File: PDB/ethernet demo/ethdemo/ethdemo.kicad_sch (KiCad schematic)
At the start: 100 parts, among them J1 0826-1X1T-GJ-F, J2 0826-1X1T-GJ-F, J3 Conn_01x05_Socket, J4 2171790001, Q1 CSD19538Q3AT, U1 STM32H742VGTx, U2 KSZ8863RLLI, U3 TPS23861PWR, Y1 25MHz

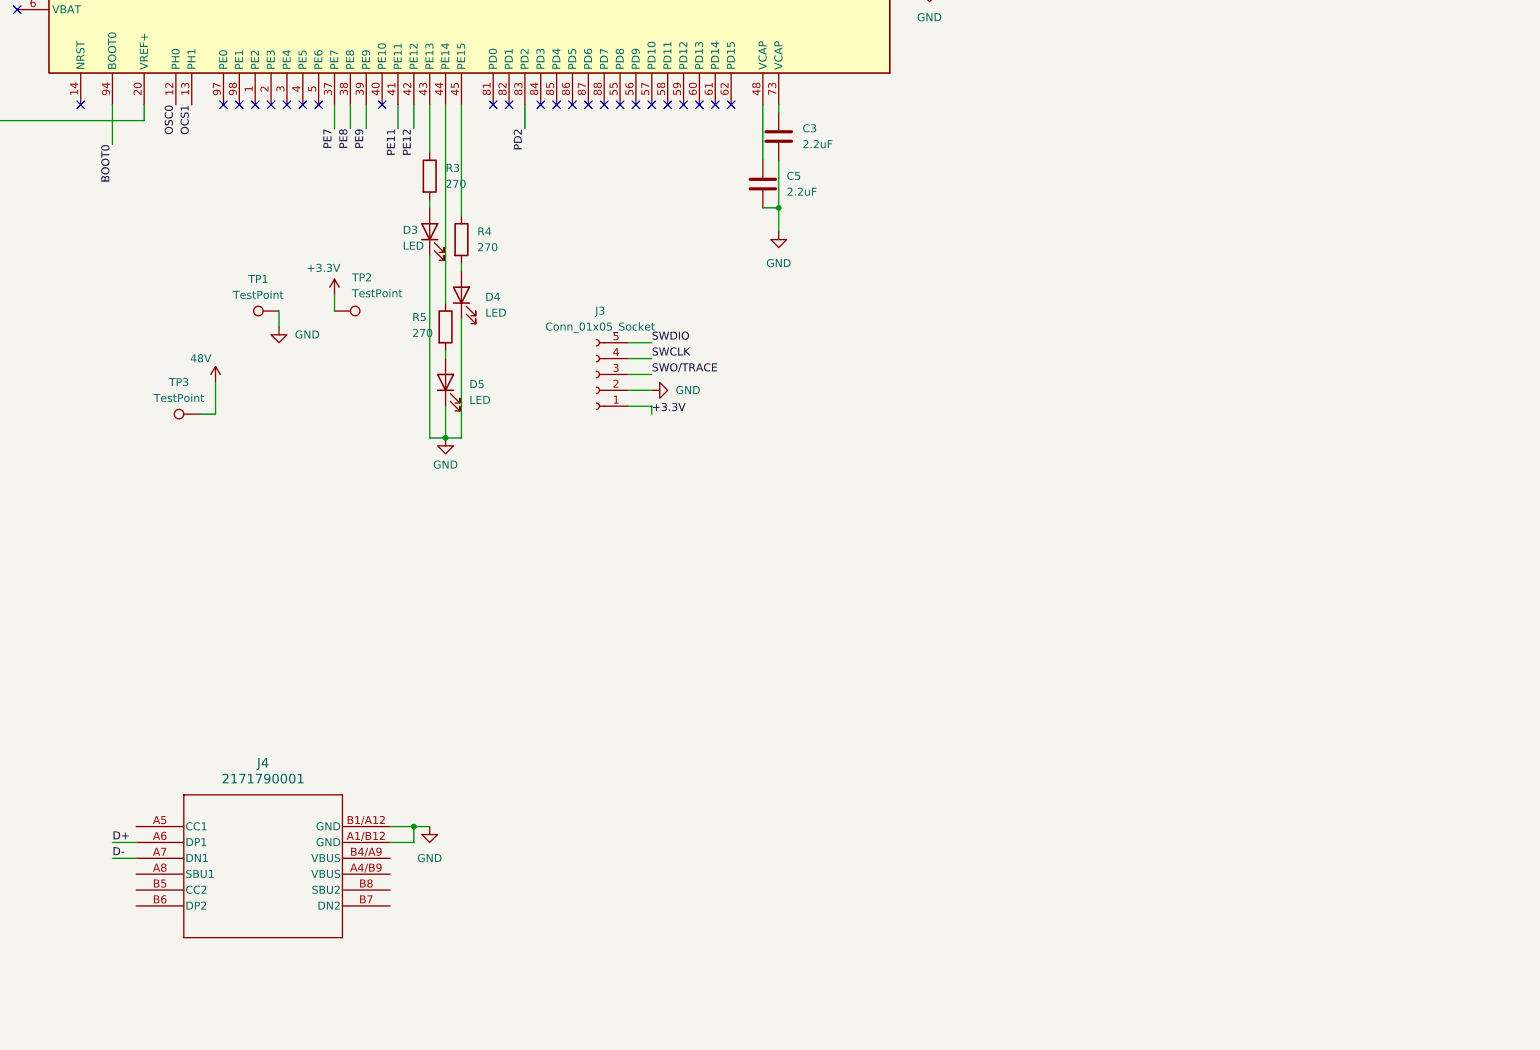
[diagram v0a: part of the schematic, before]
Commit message: routed usb and added power pads
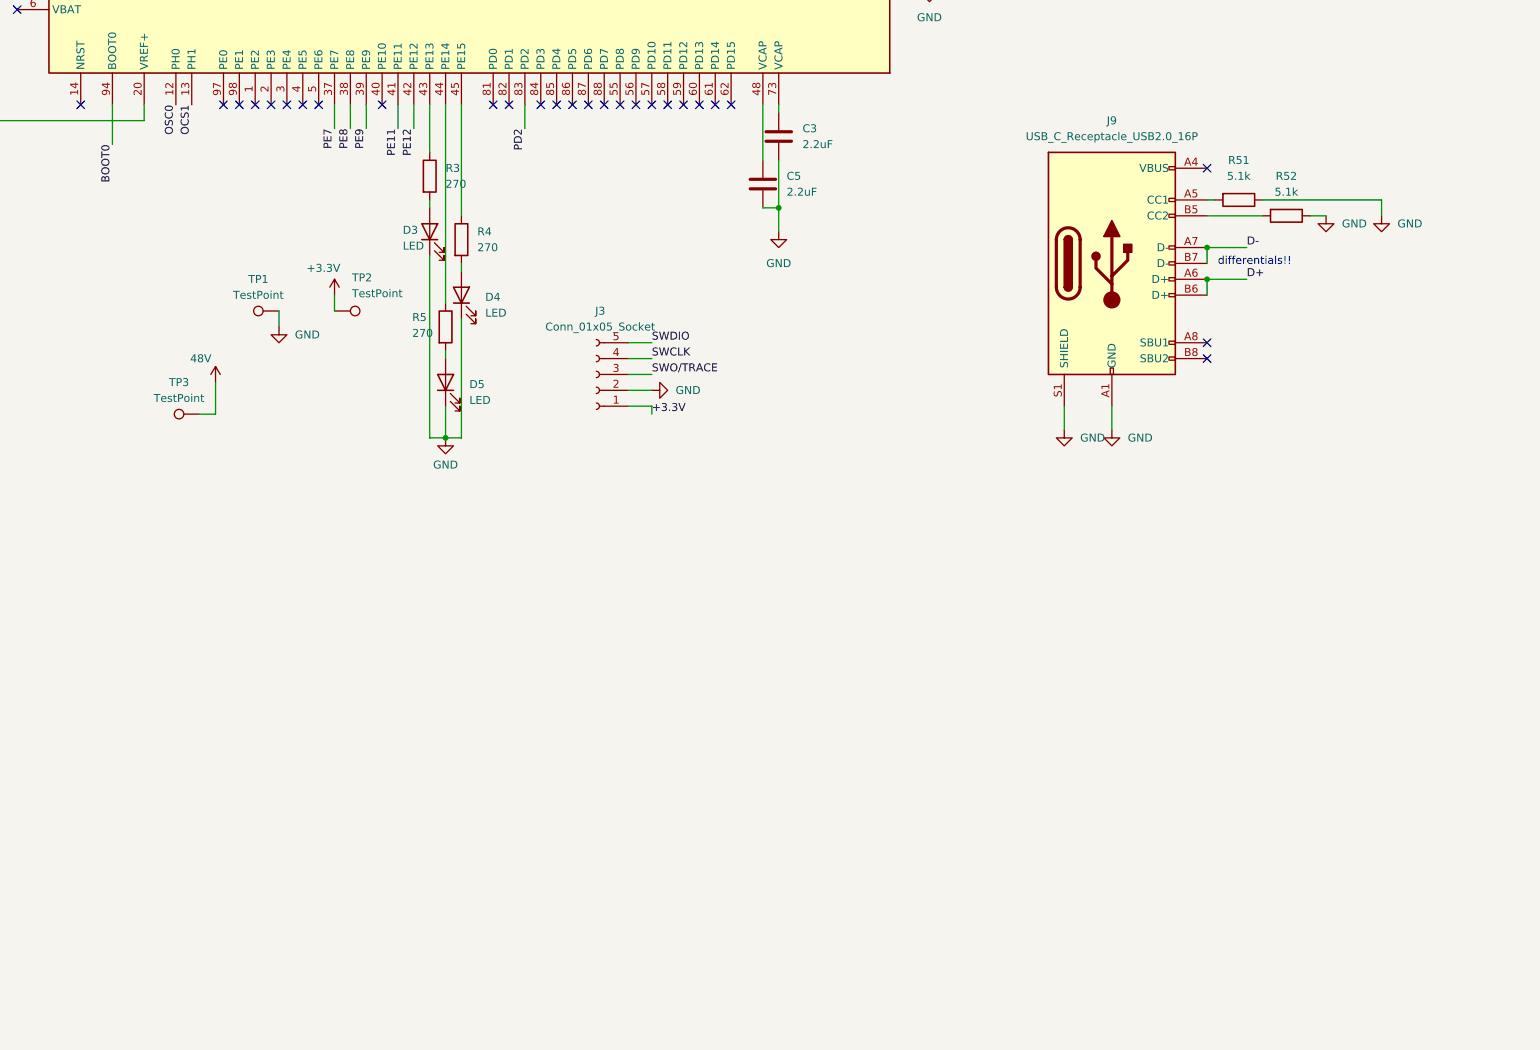
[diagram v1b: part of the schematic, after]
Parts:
- removed J4: 2171790001, 2171790001_MOL, symbol sym&foot:2171790001
- added J9: USB_C_Receptacle_USB2.0_16P, Connector_USB:USB_C_Receptacle_GCT_USB4105-xx-A_16P_TopMnt_Horizontal, symbol Connector:USB_C_Receptacle_USB2.0_16P
- added R51, R52: 5.1k, Resistor_SMD:R_0603_1608Metric_Pad0.98x0.95mm_HandSolder, symbol Device:R
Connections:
- net D+: now also J9.A6 (D+), J9.B6 (D+)
- net D-: now also J9.A7 (D-), J9.B7 (D-)
- net GND: now also J9.A1 (GND), J9.A12 (GND), J9.B1 (GND), J9.B12 (GND), J9.S1 (SHIELD), R51.1, R52.1
- new net: J9.A4 (VBUS), J9.A9 (VBUS), J9.B4 (VBUS), J9.B9 (VBUS)
- new net: J9.A5 (CC1), R51.2
- new net: J9.B5 (CC2), R52.2
- no-connect marks 59 -> 62
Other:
- note added: "differentials!!"
